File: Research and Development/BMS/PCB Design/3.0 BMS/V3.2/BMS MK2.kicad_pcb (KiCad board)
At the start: 2 copper layers, 26 parts, among them J13 CHG VCCs, J4 Batt +, J7 Batt -, J9 CHG GND, Q1 AO3400A, Q2 PN100, Q7 PN100, U1 MP1584, U3 TPS61040DBV, U4 ATTiny 85 Module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

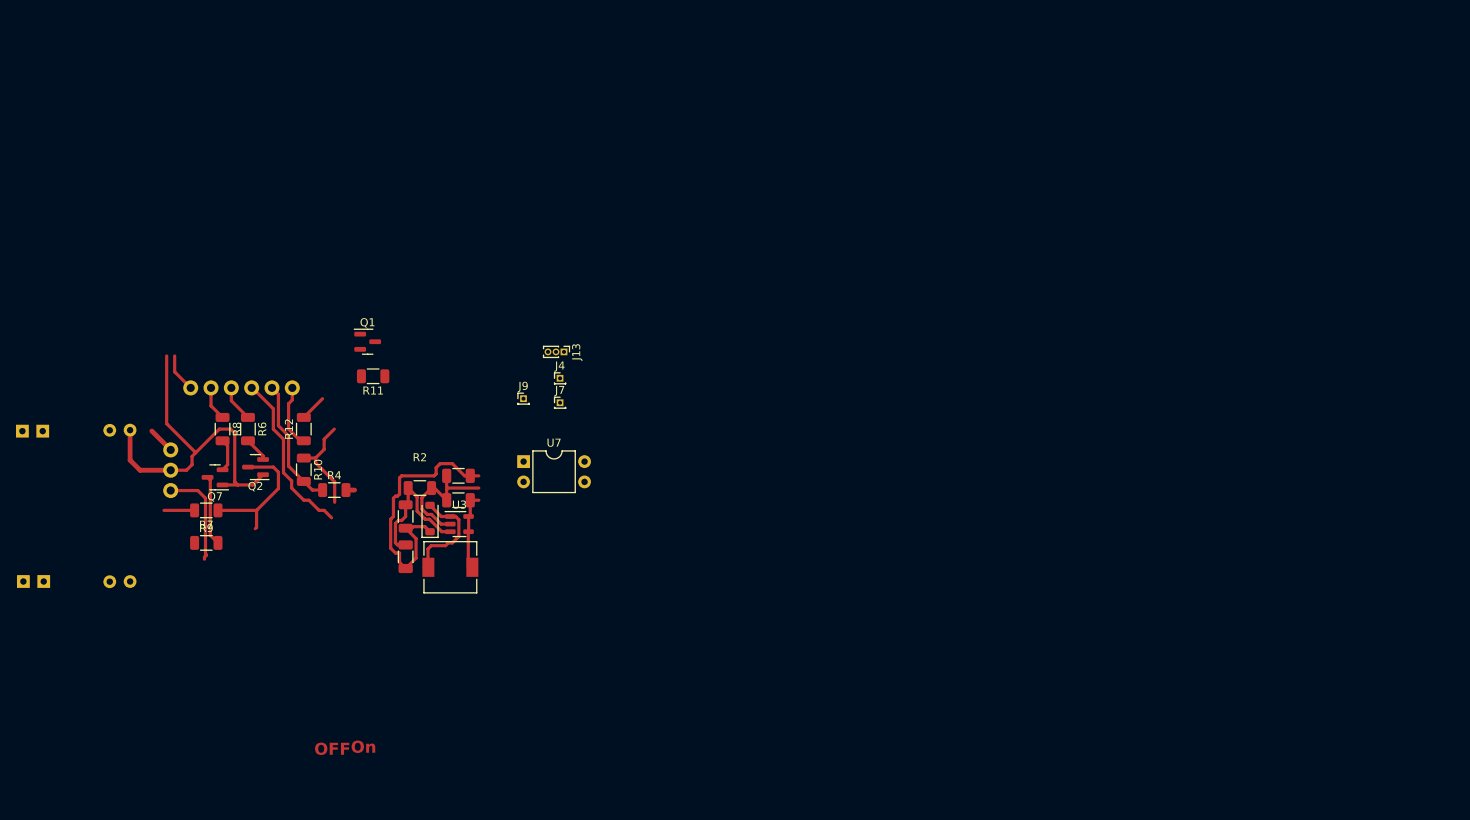
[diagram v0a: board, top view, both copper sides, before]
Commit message: Finalised BMS  schematic befeore testing PCB
is rough design without considering guitar dimension, little EMI considerations. not all concepts in design have been ensured to work properly. will test each sections viability before testing entire Circuit.

first design with the batterys and the circuit on the same board. initially had the idea of a 3d printed holder for the cells and a board on top.
 then 3 layers of single sided pcbs triple deckered with smd battery mounts. finally to this style.
although the board is larger in width and length, the height is reduced which should permit a slot in battery design for the guitar rather than a large module with a rail on the side of the guitar for battery to connect to.
This should make the design simpler and will look nicer becasue there will only be a small plastic plate exposed, rather than a chunk of the guitar body being plastic, ruining the over all finish of the guitar.
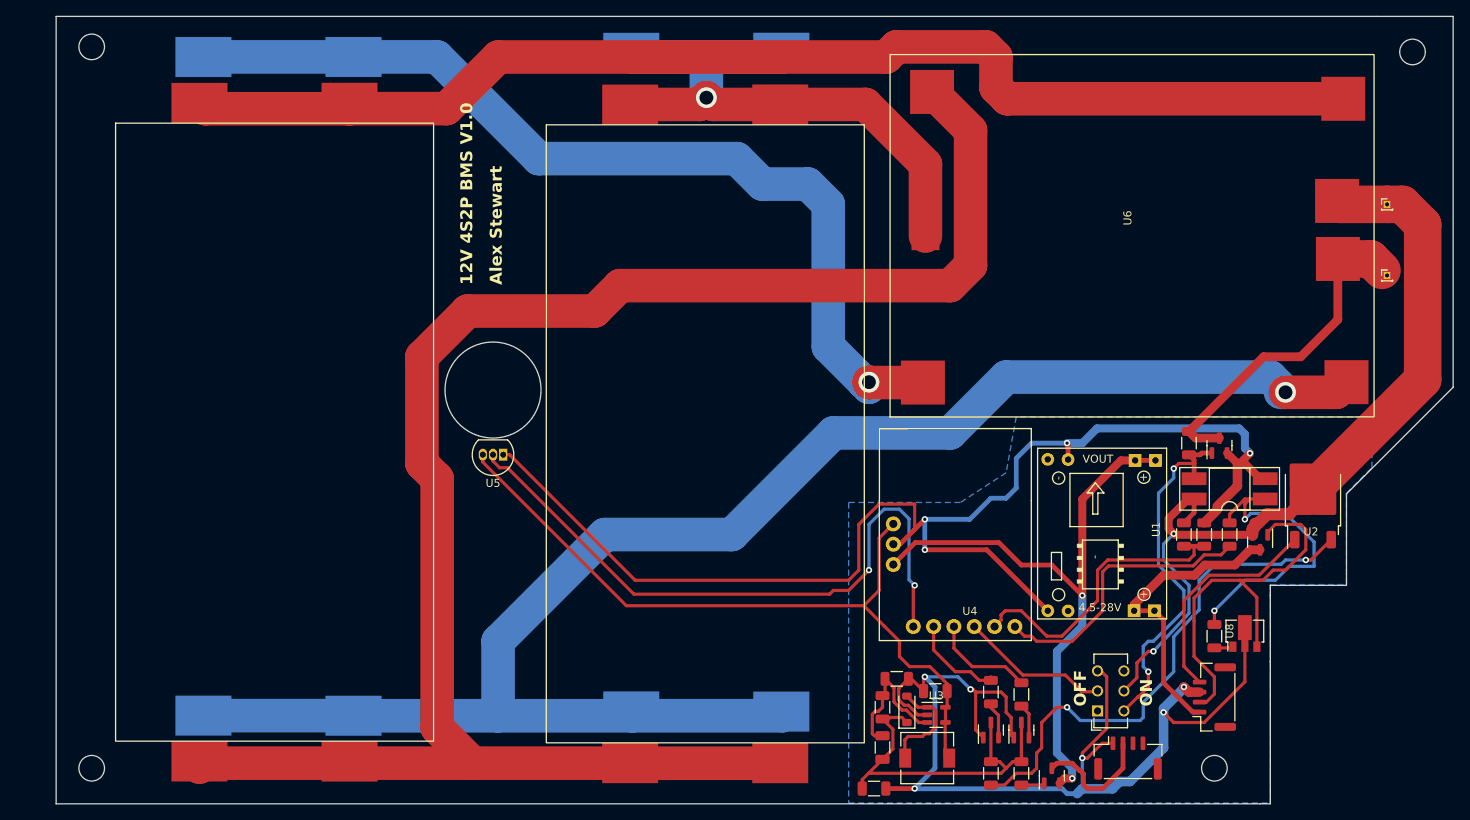
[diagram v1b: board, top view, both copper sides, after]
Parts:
- removed J13: CHG VCCs, Connector_PinHeader_1.00mm:PinHeader_1x03_P1.00mm_Vertical
- removed J9: CHG GND, Connector_PinHeader_1.00mm:PinHeader_1x01_P1.00mm_Vertical
- added B1: ~, DCDC buck converter lm2596:18650 Batt 2S Holder, B.Cu at (77.1, 59.1)
- added B2: ~, DCDC buck converter lm2596:18650 Batt 2S Holder, B.Cu at (130.6, 58.6)
- added B3: ~, DCDC buck converter lm2596:18650 Batt 2S Holder, F.Cu at (130.5, 142.4)
- added B4: ~, DCDC buck converter lm2596:18650 Batt 2S Holder, F.Cu at (76.6, 142.2)
- added J1: JST CONN OUT, Connector_JST:JST_GH_SM04B-GHS-TB_1x04-1MP_P1.25mm_Horizontal, F.Cu at (196.2, 144.2)
- added J3: JST CONN IN, Connector_JST:JST_GH_SM04B-GHS-TB_1x04-1MP_P1.25mm_Horizontal, F.Cu at (207.0, 136.6)
- added Q3: AO3407, Package_TO_SOT_SMD:SOT-23, F.Cu at (186.7, 146.5)
- added Q4: AO3407, Package_TO_SOT_SMD:SOT-23, F.Cu at (212.7, 117.3)
- added R3: 430R, Resistor_SMD:R_1206_3216Metric, F.Cu at (207.0, 129.0)
- added REF**: MountingHole_3.2mm_M3, MountingHole:MountingHole_3.2mm_M3, F.Cu at (66.7, 145.5)
- added REF**: MountingHole_3.2mm_M3, MountingHole:MountingHole_3.2mm_M3, F.Cu at (231.8, 56.0)
- added REF**: MountingHole_3.2mm_M3, MountingHole:MountingHole_3.2mm_M3, F.Cu at (207.0, 145.5)
- added REF**: MountingHole_3.2mm_M3, MountingHole:MountingHole_3.2mm_M3, F.Cu at (66.7, 55.3)
- added SW1: SW_DPDT_x2, Button_Switch_THT:SW_CuK_JS202011CQN_DPDT_Straight, F.Cu at (192.4, 138.3)
- added U2: ~, Package_TO_SOT_SMD:TO-252-2, F.Cu at (219.3, 111.9)
- added U5: DS18B20, Package_TO_SOT_THT:TO-92_Inline, F.Cu at (118.1, 106.3)
- added U6: 4s Batt Protect Module, DCDC buck converter lm2596:BMS 4S Module, F.Cu at (227.0, 101.7)
- added U8: L78L05_SOT89, Package_TO_SOT_SMD:SOT-89-3, F.Cu at (210.8, 128.4)
- J4: value Batt + -> B+
- J7: value Batt - -> B-
- U1, U4: moved to F.Cu
- U7: footprint Package_DIP:DIP-4_W7.62mm -> Package_DIP:DIP-4_W8.89mm_SMDSocket_LongPads
- moved U1 127.2 mm to (192.4, 115.7)
- moved R12 116.5 mm to (208.9, 116.3)
- moved R10 112.8 mm to (205.7, 116.3)
- moved Q1 107.3 mm to (207.6, 105.2), turned to 90 degrees
- moved R7 107.1 mm to (182.9, 146.2), turned to -90 degrees
- moved R4 106.3 mm to (203.2, 116.3), turned to 90 degrees
- moved J4 105.6 mm to (228.6, 75.0)
- moved J7 104.6 mm to (228.6, 83.9)
- moved R11 102.3 mm to (203.8, 104.9), turned to -90 degrees
- moved R9 102.2 mm to (179.1, 146.2), turned to 90 degrees
- moved R6 102.2 mm to (182.9, 136.3), turned to 90 degrees
- moved Q7 102.0 mm to (179.1, 140.7), turned to 90 degrees
- moved R8 101.5 mm to (179.1, 136.0)
- moved Q2 101.2 mm to (182.9, 140.7), turned to 90 degrees
- moved U4 95.1 mm to (175.7, 127.8)
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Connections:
- C5 pad 2: 15v+ DCHG VCC -> 15v+ CHG VCC
- C6 pad 2: 15v+ DCHG VCC -> 15v+ CHG VCC
- D1 pad 1: 15v+ DCHG VCC -> 15v+ CHG VCC
- Q2 pad 3: 15v+ DCHG VCC -> 15v+ CHG VCC
- R1 pad 1: 15v+ DCHG VCC -> 15v+ CHG VCC
- R6 pad 1: Net-(U4-P2) -> Net-(Q2-B)
- R6 pad 2: Net-(Q2-B) -> Net-(U4-P2)
- R7 pad 1: 15v+ DCHG VCC -> 15v+ CHG VCC
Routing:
- net GND: track 74.9 -> 304.4 mm, vias 0 -> 10
- net Net-(B3-B1-): track 0.00 -> 223.5 mm
- net Net-(B1-B1-): track 0.00 -> 203.4 mm, vias 0 -> 1
- net Net-(B4-B1-): track 0.00 -> 151.4 mm
- net Net-(B1-B1+): track 0.00 -> 119.6 mm, vias 0 -> 1
- net Batt +: track 1.08 -> 103.7 mm, vias 0 -> 2
- net Net-(U4-P0): track 4.82 -> 81.3 mm, vias 0 -> 2
- net Reg Batt 9v: track 3.34 -> 77.5 mm, vias 0 -> 2
- net Net-(B2-B1-): track 0.00 -> 73.8 mm, vias 0 -> 1
- net 5v attiny out: track 22.1 -> 92.7 mm
- net CGE SW VCC: track 0.09 -> 65.5 mm, vias 0 -> 2
- net 15v+ DCHG VCC: track 51.1 -> 0.00 mm
- net Chgr sgl 15V+: track 0.00 -> 49.3 mm
- net Net-(Q1-G): track 0.00 -> 45.6 mm, vias 0 -> 2
- net Batt -: track 0.00 -> 42.5 mm
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- added copper zone on B.Cu, net GND
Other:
- board outline added: 174.6 x 98.4 mm
- board text added: "12V 4S2P BMS V1.0"
- board text added: "Alex Stewart"
- board text added: "ON"
- board text removed: "On"
